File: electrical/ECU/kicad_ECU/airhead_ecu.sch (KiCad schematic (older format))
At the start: 6 parts, among them P1 CONN_01X04, P2 CONN_01X04

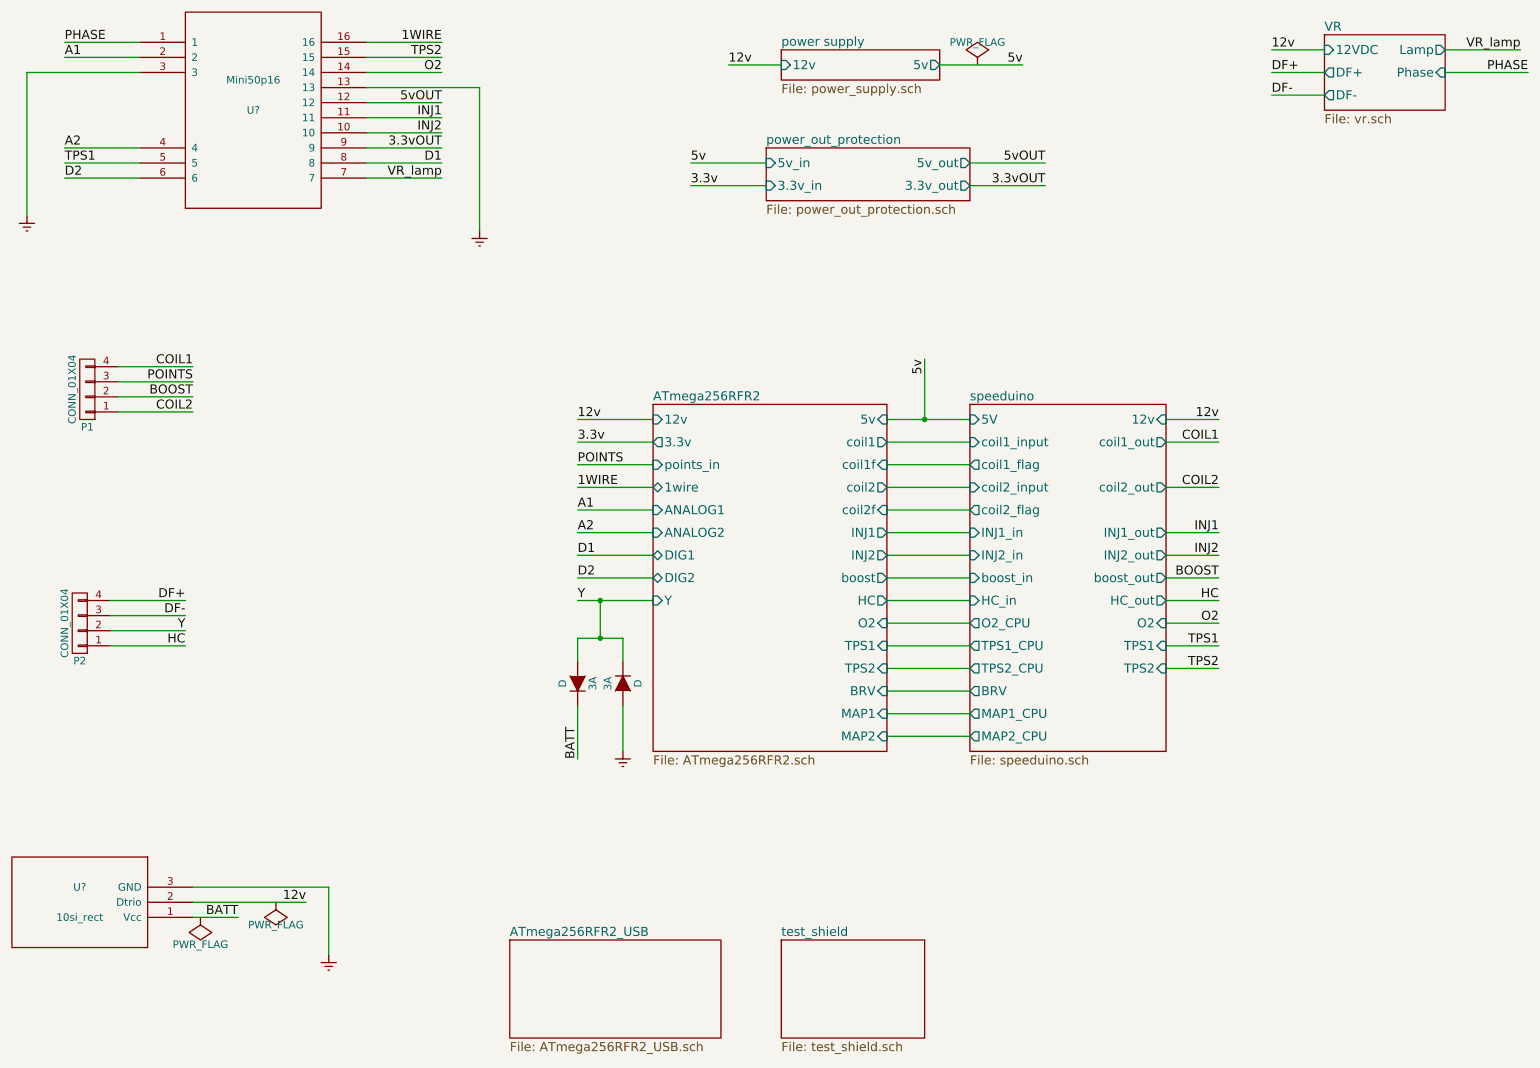
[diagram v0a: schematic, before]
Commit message: fixed some naming errors and initial round of double checking
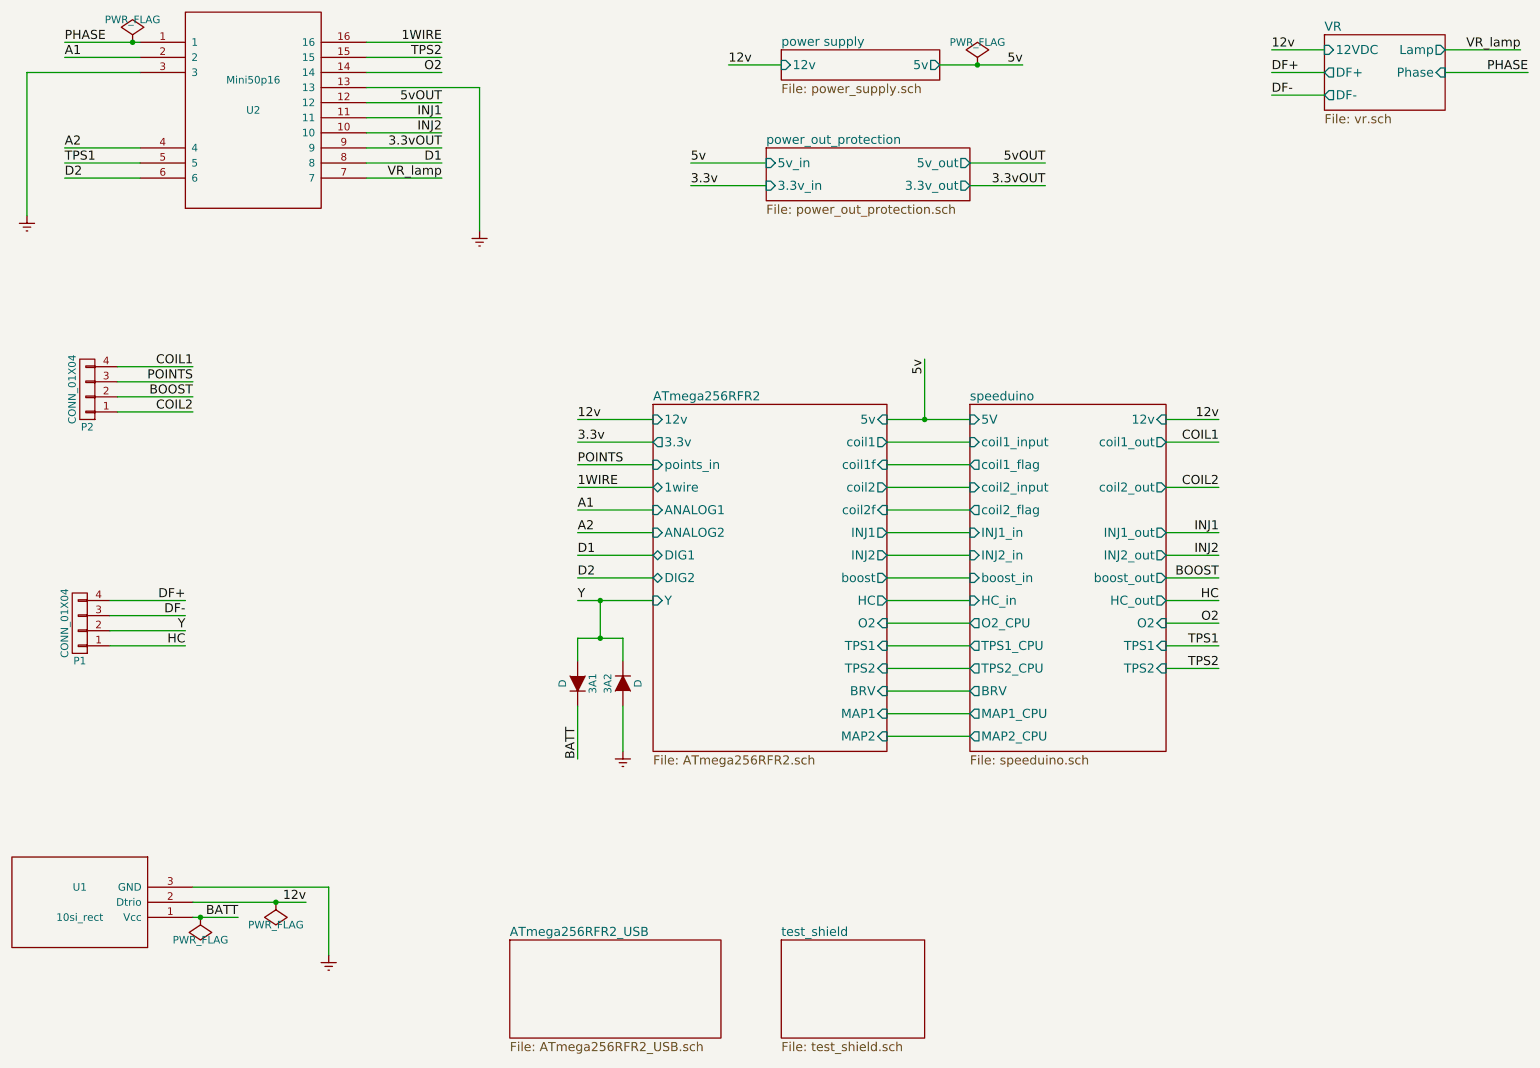
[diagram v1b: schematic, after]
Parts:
- gave numbers to parts that had none: 2
- renumbered 3A to 3A1, 3A to 3A2, P2 to P1, P1 to P2
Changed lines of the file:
@@
 $EndDescr
 $Comp
-L D 3A
+L D 3A1
 U 1 1 58897A54
 P 4400 5200
-F 0 "3A" H 4400 5300 50  0000 C CNN
+F 0 "3A1" H 4400 5300 50  0000 C CNN
 F 1 "D" H 4400 5100 50  0000 C CNN
 F 2 "" H 4400 5200 50  0000 C CNN
@@
 $EndComp
 $Comp
-L D 3A
+L D 3A2
 U 1 1 58897A8D
 P 4700 5200
-F 0 "3A" H 4700 5300 50  0000 C CNN
+F 0 "3A2" H 4700 5300 50  0000 C CNN
 F 1 "D" H 4700 5100 50  0000 C CNN
 F 2 "" H 4700 5200 50  0000 C CNN
@@
 $EndComp
 $Comp
-L CONN_01X04 P2
+L CONN_01X04 P1
 U 1 1 58977F64
 P 1100 4800
-F 0 "P2" H 1100 5050 50  0000 C CNN
+F 0 "P1" H 1100 5050 50  0000 C CNN
 F 1 "CONN_01X04" V 1200 4800 50  0000 C CNN
 F 2 "" H 1100 4800 50  0000 C CNN
@@
 $EndComp
 $Comp
-L CONN_01X04 P1
+L CONN_01X04 P2
 U 1 1 58977F99
 P 1150 3250
-F 0 "P1" H 1150 3500 50  0000 C CNN
+F 0 "P2" H 1150 3500 50  0000 C CNN
 F 1 "CONN_01X04" V 1250 3250 50  0000 C CNN
 F 2 "" H 1150 3250 50  0000 C CNN
@@
 $EndComp
 $Comp
-L Earth #PWR010
+L Earth #PWR4
 U 1 1 5898F0D8
 P 4700 5650
-F 0 "#PWR010" H 4700 5400 50  0001 C CNN
+F 0 "#PWR4" H 4700 5400 50  0001 C CNN
 F 1 "Earth" H 4700 5500 50  0001 C CNN
 F 2 "" H 4700 5650 50  0000 C CNN
@@
 	1    4700 5650
 	-1   0    0    -1
-$EndComp
-$Comp
-L PWR_FLAG #FLG020
-U 1 1 589EC0CC
-P 1900 6750
-F 0 "#FLG020" H 1900 6845 50  0001 C CNN
-F 1 "PWR_FLAG" H 1900 6930 50  0000 C CNN
-F 2 "" H 1900 6750 50  0000 C CNN
-F 3 "" H 1900 6750 50  0000 C CNN
-	1    1900 6750
-	1    0    0    1
 $EndComp
 $Sheet
@@
 12v
 $Comp
-L 10si_rect U?
+L 10si_rect U1
 U 1 1 597E65C7
 P 1100 6650
-F 0 "U?" H 1100 6550 50  0000 C CNN
+F 0 "U1" H 1100 6550 50  0000 C CNN
 F 1 "10si_rect" H 1100 6750 50  0000 C CNN
 F 2 "MODULE" H 1100 6650 50  0001 C CNN
@@
 12v
 $Comp
-L PWR_FLAG #FLG?
+L PWR_FLAG #FLG3
 U 1 1 597E73C4
 P 2400 6650
-F 0 "#FLG?" H 2400 6725 50  0001 C CNN
+F 0 "#FLG3" H 2400 6725 50  0001 C CNN
 F 1 "PWR_FLAG" H 2400 6800 50  0000 C CNN
 F 2 "" H 2400 6650 50  0001 C CNN
@@
 	-1   0    0    1
 $EndComp
-Text Label 2150 6750 2    60   ~ 0
-BATT
-$Comp
-L Earth #PWR?
+$Comp
+L Earth #PWR2
 U 1 1 597E7602
 P 2750 7000
-F 0 "#PWR?" H 2750 6750 50  0001 C CNN
+F 0 "#PWR2" H 2750 6750 50  0001 C CNN
 F 1 "Earth" H 2750 6850 50  0001 C CNN
 F 2 "" H 2750 7000 50  0001 C CNN
@@
 Text Label 10650 1000 2    60   ~ 0
 VR_lamp
-$Comp
-L PWR_FLAG #FLG?
-U 1 1 597EFDD6
-P 7050 1100
-F 0 "#FLG?" H 7050 1175 50  0001 C CNN
-F 1 "PWR_FLAG" H 7050 1250 50  0000 C CNN
-F 2 "" H 7050 1100 50  0001 C CNN
-F 3 "" H 7050 1100 50  0001 C CNN
-	1    7050 1100
-	1    0    0    -1
-$EndComp
 Wire Wire Line
 	4400 5050 4400 4900
@@
 Wire Wire Line
 	1850 6650 2600 6650
-Wire Wire Line
-	1850 6750 2150 6750
 Wire Wire Line
 	1850 6550 2750 6550
@@
 Connection ~ 4550 4650
 $Comp
-L Mini50p16 U?
+L Mini50p16 U2
 U 1 1 59804CF3
 P 2250 1400
-F 0 "U?" H 2250 1400 50  0000 C CNN
+F 0 "U2" H 2250 1400 50  0000 C CNN
 F 1 "Mini50p16" H 2250 1600 50  0000 C CNN
 F 2 "MODULE" H 2250 1500 50  0001 C CNN
@@
 	750  1150 750  2100
 $Comp
-L Earth #PWR?
+L Earth #PWR1
 U 1 1 598074B3
 P 750 2100
-F 0 "#PWR?" H 750 1850 50  0001 C CNN
+F 0 "#PWR1" H 750 1850 50  0001 C CNN
 F 1 "Earth" H 750 1950 50  0001 C CNN
 F 2 "" H 750 2100 50  0001 C CNN
@@
 	3750 1250 3750 2200
 $Comp
-L Earth #PWR?
+L Earth #PWR3
 U 1 1 59807753
 P 3750 2200
-F 0 "#PWR?" H 3750 1950 50  0001 C CNN
+F 0 "#PWR3" H 3750 1950 50  0001 C CNN
 F 1 "Earth" H 3750 2050 50  0001 C CNN
 F 2 "" H 3750 2200 50  0001 C CNN
@@
 Wire Wire Line
 	7500 1750 7000 1750
+Wire Wire Line
+	1850 6750 2150 6750
+Text Label 2150 6750 2    60   ~ 0
+BATT
+Connection ~ 2400 6650
+$Comp
+L PWR_FLAG #FLG2
+U 1 1 5990DA86
+P 1900 6750
+F 0 "#FLG2" H 1900 6825 50  0001 C CNN
+F 1 "PWR_FLAG" H 1900 6900 50  0000 C CNN
+F 2 "" H 1900 6750 50  0001 C CNN
+F 3 "" H 1900 6750 50  0001 C CNN
+	1    1900 6750
+	-1   0    0    1
+$EndComp
+Connection ~ 1900 6750
+$Comp
+L PWR_FLAG #FLG1
+U 1 1 5990DC10
+P 1450 950
+F 0 "#FLG1" H 1450 1025 50  0001 C CNN
+F 1 "PWR_FLAG" H 1450 1100 50  0000 C CNN
+F 2 "" H 1450 950 50  0001 C CNN
+F 3 "" H 1450 950 50  0001 C CNN
+	1    1450 950
+	1    0    0    -1
+$EndComp
+Connection ~ 1450 950
+$Comp
+L PWR_FLAG #FLG4
+U 1 1 5991C36F
+P 7050 1100
+F 0 "#FLG4" H 7050 1175 50  0001 C CNN
+F 1 "PWR_FLAG" H 7050 1250 50  0000 C CNN
+F 2 "" H 7050 1100 50  0001 C CNN
+F 3 "" H 7050 1100 50  0001 C CNN
+	1    7050 1100
+	1    0    0    -1
+$EndComp
+Connection ~ 7050 1100
 $EndSCHEMATC
